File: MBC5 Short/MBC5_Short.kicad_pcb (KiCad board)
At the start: 2 copper layers, 51 x 30.7 mm, 1 part, among them J1 GameBoy_GamePak_AGB-002

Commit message: Update board specifications/clearances for OshPark service
Even though I did all the routing with the original settings....😬
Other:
- rule pad_to_mask_clearance: 0.05 -> 0.0508
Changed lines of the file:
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@@
       (dielectric_constraints no)
     )
-    (pad_to_mask_clearance 0.05)
+    (pad_to_mask_clearance 0.0508)
+    (solder_mask_min_width 0.101)
     (pcbplotparams
       (layerselection 0x00010fc_ffffffff)

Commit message: Route entire board, bam
This was a lot of work, but I really didn't feel like doing micro-commits for all the changes here and there
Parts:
- added C1: 100nF, Capacitor_SMD:C_0603_1608Metric, F.Cu at (127.6, 108.0)
- added C2: 100nF, Capacitor_SMD:C_0603_1608Metric, F.Cu at (148.7, 92.0)
- added C3: 100nF, Capacitor_SMD:C_0603_1608Metric, F.Cu at (140.2, 88.5)
- added C4: 100nF, Capacitor_SMD:C_0603_1608Metric, F.Cu at (157.3, 88.6)
- added GNDPAD: Nintendo_2.25x2.25_Fiducial, NintendoFootprints:Nintendo_2.25x2.25_Fiducial, F.Cu at (171.5, 87.8)
- added PAD*: GB-ProductionIndicator, NintendoFootprints:GB-ProductionIndicator, B.Cu at (171.6, 103.2)
- added U1: 29F033, Package_SO:TSOP-I-40_18.4x10mm_P0.5mm, F.Cu at (164.5, 97.2)
- added U2: MBC5, Package_QFP:LQFP-32_7x7mm_P0.8mm, F.Cu at (151.0, 98.0)
- added U3: FM18W08, Package_SO:SOIC-28W_7.5x17.9mm_P1.27mm, F.Cu at (133.0, 97.5)
- added kibuzzard-622AB126: G***, kibuzzard-622AB126, B.Cu at (131.4, 88.7)
- added kibuzzard-622AB1EA: G***, kibuzzard-622AB1EA, B.Cu at (138.0, 88.9)
- added kibuzzard-622CFB3C: G***, kibuzzard-622CFB3C, F.Cu at (171.5, 98.3)
- added kibuzzard-622CFB40: G***, kibuzzard-622CFB40, F.Cu at (171.6, 98.3)
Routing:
- net RD: track 0.00 -> 77.4 mm, vias 0 -> 6
- net A12: track 0.00 -> 69.2 mm, vias 0 -> 3
- net A7: track 0.00 -> 62.8 mm, vias 0 -> 2
- net A6: track 0.00 -> 60.7 mm, vias 0 -> 2
- net A5: track 0.00 -> 58.7 mm, vias 0 -> 2
- net GND: track 0.00 -> 57.6 mm, vias 0 -> 7
- net +5V: track 0.00 -> 56.7 mm, vias 0 -> 2
- net A4: track 0.00 -> 56.3 mm, vias 0 -> 2
- net A11: track 0.00 -> 50.9 mm, vias 0 -> 2
- net A10: track 0.00 -> 49.2 mm, vias 0 -> 2
- net A9: track 0.00 -> 48.0 mm, vias 0 -> 3
- net A8: track 0.00 -> 47.9 mm, vias 0 -> 3
- net D7: track 0.00 -> 47.8 mm, vias 0 -> 2
- net D0: track 0.00 -> 47.8 mm, vias 0 -> 2
- net D1: track 0.00 -> 47.5 mm, vias 0 -> 2
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- added copper zone on F.Cu, net +5V
- added copper zone on B.Cu, net GND
- added copper zone on F.Cu, net GND
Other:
- board text added: "1"
- board text added: "32"
- board text added: "GND"
- board text added: "VCC"
- board text added: "v1"

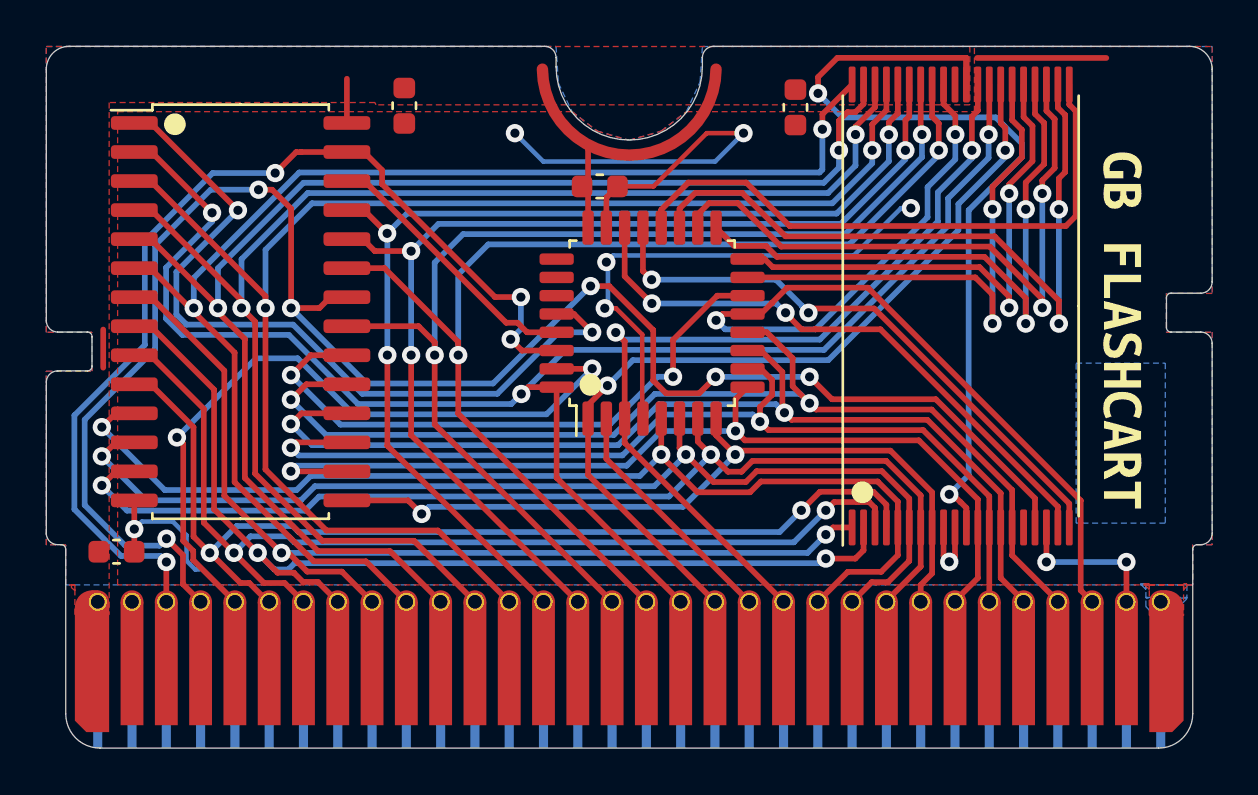
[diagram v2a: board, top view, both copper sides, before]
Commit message: Change TSOP-40 to TSOP-48 to accomodate more chip variations
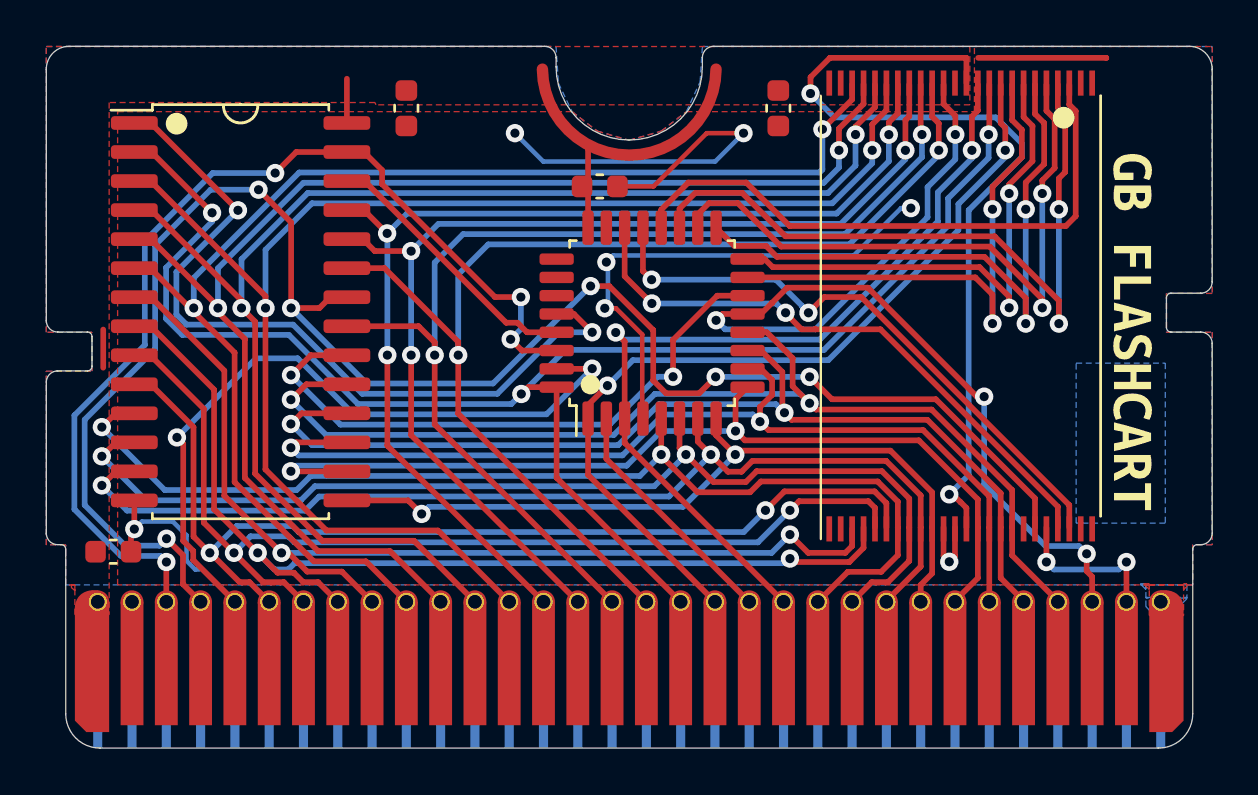
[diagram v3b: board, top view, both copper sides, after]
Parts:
- U1: value 29F033 -> 29F0; footprint Package_SO:TSOP-I-40_18.4x10mm_P0.5mm -> Package_SO:TSOP-I-48_18.4x12mm_P0.5mm
- moved GNDPAD 1.57 mm to (173.1, 87.8)
- moved C4 0.75 mm to (156.5, 88.6)
- moved kibuzzard-622CFB40 0.45 mm to (172.0, 98.4)
- moved kibuzzard-622CFB3C 0.45 mm to (172.0, 98.4)
- moved C3 0.14 mm to (140.2, 88.6)
- moved C1 0.14 mm to (127.4, 108.0)
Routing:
- net GND: track 57.6 -> 55.3 mm
- net A3: track 44.5 -> 45.6 mm
- net RESET: track 43.1 -> 44.0 mm, vias 2 -> 4
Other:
- board text added: "v2"
- board text added: "xx"
- board text removed: "v1"
